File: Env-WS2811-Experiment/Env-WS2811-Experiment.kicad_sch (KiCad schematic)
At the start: 142 parts, among them J1 Conn_01x04, Q1 Si2301DS, Q10 Si2301DS, Q11 Si2301DS, Q12 Si2301DS, Q13 Si2301DS, Q14 Si2301DS, Q15 Si2301DS, Q16 Si2301DS, Q17 Si2301DS, Q18 Si2301DS, Q19 Si2301DS, Q2 Si2301DS, Q20 Si2301DS, Q21 Si2301DS, Q22 Si2301DS, Q23 Si2301DS, Q24 Si2301DS, Q25 Si2301DS, Q26 Si2301DS, Q27 Si2301DS, Q28 Si2301DS, Q29 Si2301DS, Q3 Si2301DS, Q30 Si2301DS, Q31 Si2301DS, Q32 Si2301DS, Q33 Si2301DS, Q34 Si2301DS, Q35 Si2301DS, Q36 Si2301DS, Q4 Si2301DS, Q5 Si2301DS, Q6 Si2301DS, Q7 Si2301DS, Q8 Si2301DS, Q9 Si2301DS, U1 WS2811, U10 WS2811, U11 WS2811, U12 WS2811, U2 WS2811, U3 WS2811, U4 WS2811, U5 WS2811, U6 WS2811, U7 WS2811, U8 WS2811, U9 WS2811

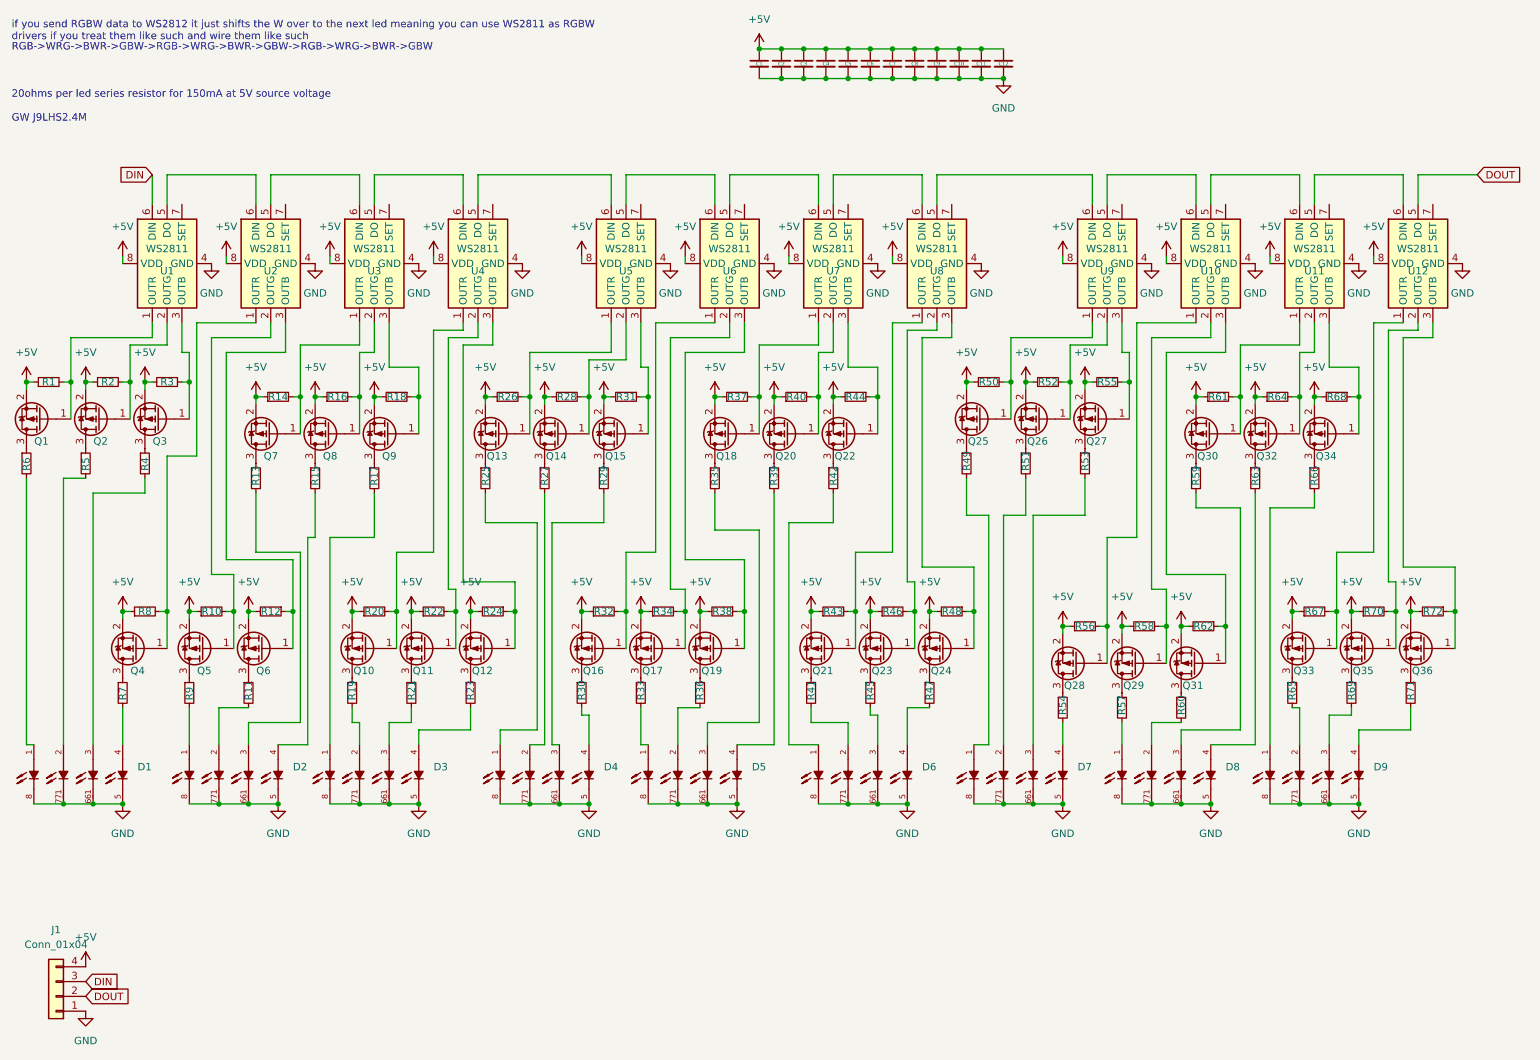
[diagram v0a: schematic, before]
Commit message: swap some mosfets over to more compact versions
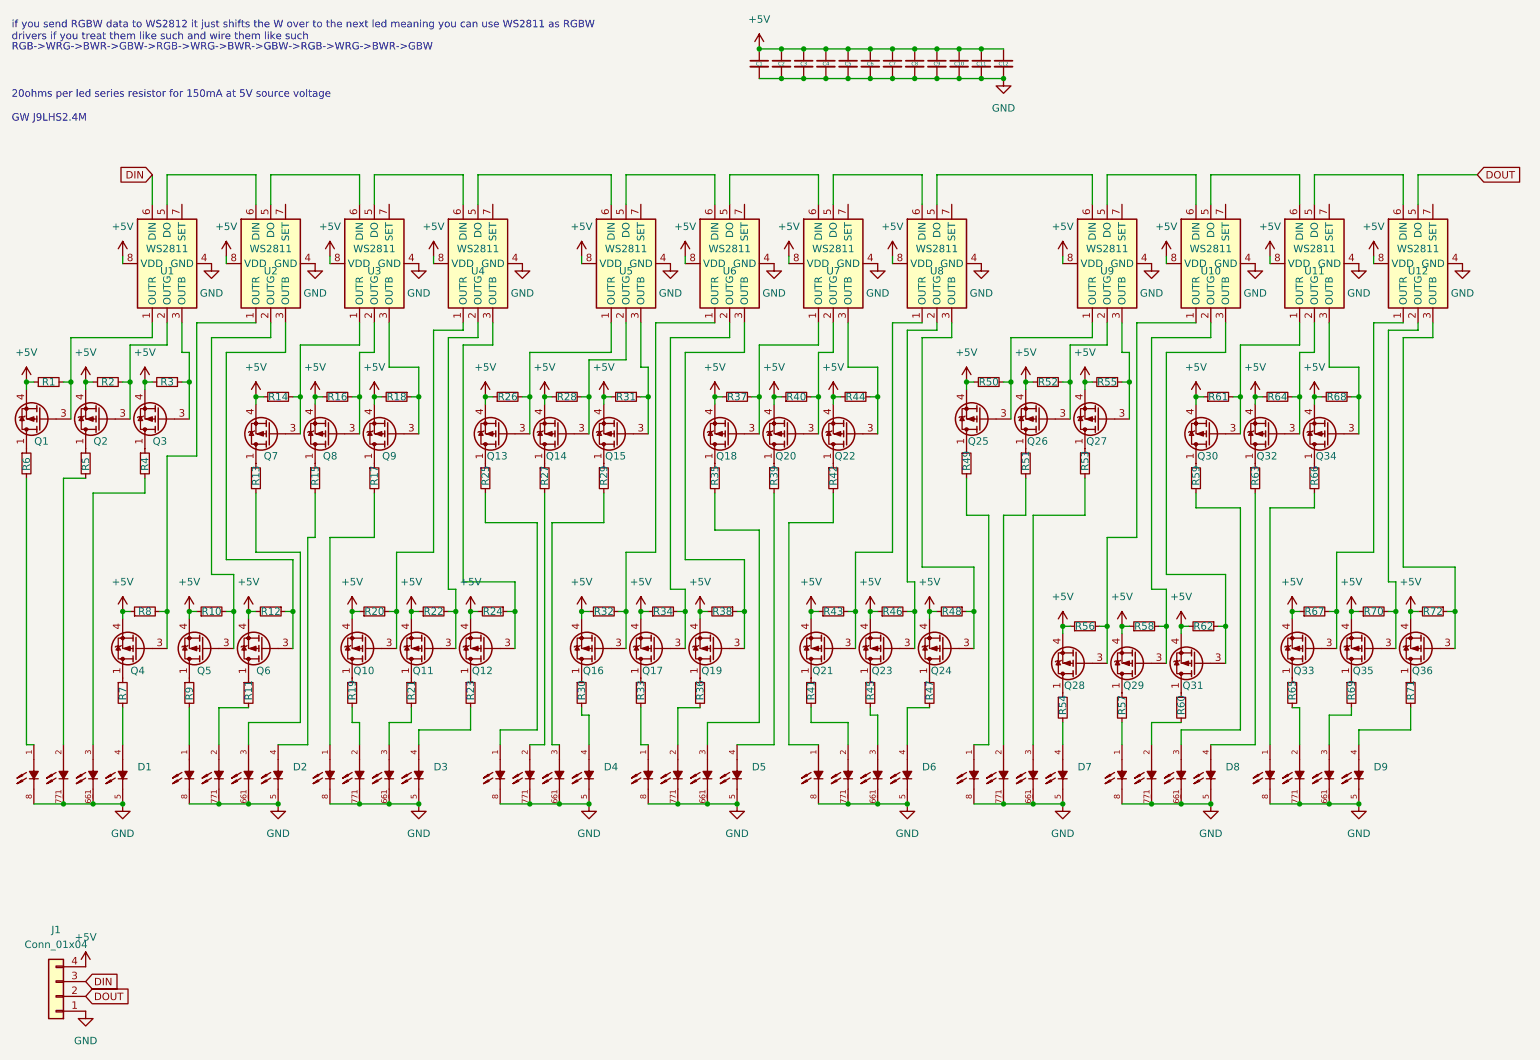
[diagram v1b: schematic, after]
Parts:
- Q1, Q10, Q11, Q12, Q13, Q14, Q15, Q16, Q17, Q18, Q19, Q2, Q20, Q21, Q22, Q23, Q24, Q25, Q26, Q27, Q28, Q29, Q3, Q30, Q31, Q32, Q33, Q34, Q35, Q36, Q4, Q5, Q6, Q7, Q8, Q9: value Si2301DS -> SIA483DJ; footprint Package_TO_SOT_SMD:SOT-23 -> Package_TO_SOT_SMD:Vishay_PowerPAK_SC70-6L_Single; symbol Transistor_FET:Si2319CDS -> Transistor_FET:SiA449DJ
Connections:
- net +5V: now also Q1.4 (S), Q10.4 (S), Q11.4 (S), Q12.4 (S), Q13.4 (S), Q14.4 (S), Q15.4 (S), Q16.4 (S), Q17.4 (S), Q18.4 (S), Q19.4 (S), Q2.4 (S), Q20.4 (S), Q21.4 (S), Q22.4 (S), Q23.4 (S), Q24.4 (S), Q25.4 (S), Q26.4 (S), Q27.4 (S), Q28.4 (S), Q29.4 (S), Q3.4 (S), Q30.4 (S), Q31.4 (S), Q32.4 (S), Q33.4 (S), Q34.4 (S), Q35.4 (S), Q36.4 (S), Q4.4 (S), Q5.4 (S), Q6.4 (S), Q7.4 (S), Q8.4 (S), Q9.4 (S); no longer Q1.2 (S), Q10.2 (S), Q11.2 (S), Q12.2 (S), Q13.2 (S), Q14.2 (S), Q15.2 (S), Q16.2 (S), Q17.2 (S), Q18.2 (S), Q19.2 (S), Q2.2 (S), Q20.2 (S), Q21.2 (S), Q22.2 (S), Q23.2 (S), Q24.2 (S), Q25.2 (S), Q26.2 (S), Q27.2 (S), Q28.2 (S), Q29.2 (S), Q3.2 (S), Q30.2 (S), Q31.2 (S), Q32.2 (S), Q33.2 (S), Q34.2 (S), Q35.2 (S), Q36.2 (S), Q4.2 (S), Q5.2 (S), Q6.2 (S), Q7.2 (S), Q8.2 (S), Q9.2 (S)
- net at R46.2, U8.2 (OUTG): now also Q23.3 (G); no longer Q23.1 (G)
- net at R14.2, U3.1 (OUTR): now also Q7.3 (G); no longer Q7.1 (G)
- net at R16.2, U3.2 (OUTG): now also Q8.3 (G); no longer Q8.1 (G)
- net at R18.1, U3.3 (OUTB): now also Q9.3 (G); no longer Q9.1 (G)
- net at R39.1: now also Q20.1 (D); no longer Q20.3 (D)
- net at R20.2, U4.1 (OUTR): now also Q10.3 (G); no longer Q10.1 (G)
- net at R22.2, U4.2 (OUTG): now also Q11.3 (G); no longer Q11.1 (G)
- net at R24.1, U4.3 (OUTB): now also Q12.3 (G); no longer Q12.1 (G)
- net at R50.2, U9.1 (OUTR): now also Q25.3 (G); no longer Q25.1 (G)
- net at R38.1, U6.3 (OUTB): now also Q19.3 (G); no longer Q19.1 (G)
- net at R21.1: now also Q11.1 (D); no longer Q11.3 (D)
- net at R32.2, U6.1 (OUTR): now also Q16.3 (G); no longer Q16.1 (G)
- net at R30.1: now also Q16.1 (D); no longer Q16.3 (D)
- net at R53.1: now also Q27.1 (D); no longer Q27.3 (D)
- net at R23.1: now also Q12.1 (D); no longer Q12.3 (D)
- net at R72.1, U12.3 (OUTB): now also Q36.3 (G); no longer Q36.1 (G)
- net at R17.1: now also Q9.1 (D); no longer Q9.3 (D)
- net at R3.1, U1.3 (OUTB): now also Q3.3 (G); no longer Q3.1 (G)
- net at R1.2, U1.1 (OUTR): now also Q1.3 (G); no longer Q1.1 (G)
- net at R2.2, U1.2 (OUTG): now also Q2.3 (G); no longer Q2.1 (G)
- net at R31.1, U5.3 (OUTB): now also Q15.3 (G); no longer Q15.1 (G)
- net at R55.1, U9.3 (OUTB): now also Q27.3 (G); no longer Q27.1 (G)
- net at R67.2, U12.1 (OUTR): now also Q33.3 (G); no longer Q33.1 (G)
- net at R65.1: now also Q33.1 (D); no longer Q33.3 (D)
- net at R15.1: now also Q8.1 (D); no longer Q8.3 (D)
- net at R56.2, U10.1 (OUTR): now also Q28.3 (G); no longer Q28.1 (G)
- net at R54.1: now also Q28.1 (D); no longer Q28.3 (D)
- net at R61.2, U11.1 (OUTR): now also Q30.3 (G); no longer Q30.1 (G)
- net at R64.2, U11.2 (OUTG): now also Q32.3 (G); no longer Q32.1 (G)
- net at R68.1, U11.3 (OUTB): now also Q34.3 (G); no longer Q34.1 (G)
- net at R49.1: now also Q25.1 (D); no longer Q25.3 (D)
- net at R45.1: now also Q23.1 (D); no longer Q23.3 (D)
- net at R70.2, U12.2 (OUTG): now also Q35.3 (G); no longer Q35.1 (G)
- net at R34.2, U6.2 (OUTG): now also Q17.3 (G); no longer Q17.1 (G)
- net at R71.1: now also Q36.1 (D); no longer Q36.3 (D)
- net at R19.1: now also Q10.1 (D); no longer Q10.3 (D)
- net at R58.2, U10.2 (OUTG): now also Q29.3 (G); no longer Q29.1 (G)
- net at R57.1: now also Q29.1 (D); no longer Q29.3 (D)
- net at R41.1: now also Q21.1 (D); no longer Q21.3 (D)
- net at R5.1: now also Q2.1 (D); no longer Q2.3 (D)
- net at R12.1, U2.3 (OUTB): now also Q6.3 (G); no longer Q6.1 (G)
- net at R11.1: now also Q6.1 (D); no longer Q6.3 (D)
- net at R62.1, U10.3 (OUTB): now also Q31.3 (G); no longer Q31.1 (G)
- net at R36.1: now also Q19.1 (D); no longer Q19.3 (D)
- net at R63.1: now also Q32.1 (D); no longer Q32.3 (D)
- net at R26.2, U5.1 (OUTR): now also Q13.3 (G); no longer Q13.1 (G)
- net at R25.1: now also Q13.1 (D); no longer Q13.3 (D)
- net at R10.2, U2.2 (OUTG): now also Q5.3 (G); no longer Q5.1 (G)
- net at R9.1: now also Q5.1 (D); no longer Q5.3 (D)
- net at R33.1: now also Q17.1 (D); no longer Q17.3 (D)
- net at R13.1: now also Q7.1 (D); no longer Q7.3 (D)
- net at R28.2, U5.2 (OUTG): now also Q14.3 (G); no longer Q14.1 (G)
- net at R27.1: now also Q14.1 (D); no longer Q14.3 (D)
- net at R43.2, U8.1 (OUTR): now also Q21.3 (G); no longer Q21.1 (G)
- net at R8.2, U2.1 (OUTR): now also Q4.3 (G); no longer Q4.1 (G)
- net at R51.1: now also Q26.1 (D); no longer Q26.3 (D)
- net at R47.1: now also Q24.1 (D); no longer Q24.3 (D)
- net at R52.2, U9.2 (OUTG): now also Q26.3 (G); no longer Q26.1 (G)
- net at R66.1: now also Q34.1 (D); no longer Q34.3 (D)
- net at R6.1: now also Q1.1 (D); no longer Q1.3 (D)
- net at R40.2, U7.2 (OUTG): now also Q20.3 (G); no longer Q20.1 (G)
- net at R37.2, U7.1 (OUTR): now also Q18.3 (G); no longer Q18.1 (G)
- net at R7.1: now also Q4.1 (D); no longer Q4.3 (D)
- net at R48.1, U8.3 (OUTB): now also Q24.3 (G); no longer Q24.1 (G)
- net at R44.1, U7.3 (OUTB): now also Q22.3 (G); no longer Q22.1 (G)
- net at R4.1: now also Q3.1 (D); no longer Q3.3 (D)
- net at R35.1: now also Q18.1 (D); no longer Q18.3 (D)
- net at R60.1: now also Q31.1 (D); no longer Q31.3 (D)
- net at R69.1: now also Q35.1 (D); no longer Q35.3 (D)
- net at R42.1: now also Q22.1 (D); no longer Q22.3 (D)
- net at R59.1: now also Q30.1 (D); no longer Q30.3 (D)
- net at R29.1: now also Q15.1 (D); no longer Q15.3 (D)
